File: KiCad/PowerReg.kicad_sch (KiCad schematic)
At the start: 5 parts, among them U2 TPS62162DSG

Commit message: did I really just do the whole thing in one commit
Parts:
- removed R6: 100k, Resistor_SMD:R_0402_1005Metric, symbol Device:R
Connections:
- net PG is gone; now on net GND: U2.8 (PG)
- net +BATT renamed +VDC
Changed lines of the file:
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@@
 	(paper "A4")
+	(junction
+		(at 123.19 77.47)
+		(diameter 0)
+		(color 0 0 0 0)
+	)
+	(junction
+		(at 120.65 77.47)
+		(diameter 0)
+		(color 0 0 0 0)
+	)
+	(junction
+		(at 175.26 63.5)
+		(diameter 0)
+		(color 0 0 0 0)
+	)
+	(junction
+		(at 143.51 57.15)
+		(diameter 0)
+		(color 0 0 0 0)
+	)
+	(junction
+		(at 175.26 55.88)
+		(diameter 0)
+		(color 0 0 0 0)
+	)
 	(junction
 		(at 100.33 57.15)
@@
 		(color 0 0 0 0)
 	)
-	(junction
-		(at 123.19 77.47)
-		(diameter 0)
-		(color 0 0 0 0)
-	)
-	(junction
-		(at 120.65 77.47)
-		(diameter 0)
-		(color 0 0 0 0)
-	)
-	(junction
-		(at 175.26 63.5)
-		(diameter 0)
-		(color 0 0 0 0)
-	)
-	(junction
-		(at 143.51 59.69)
-		(diameter 0)
-		(color 0 0 0 0)
-	)
-	(junction
-		(at 143.51 57.15)
-		(diameter 0)
-		(color 0 0 0 0)
-	)
-	(junction
-		(at 175.26 55.88)
-		(diameter 0)
-		(color 0 0 0 0)
-	)
 	(wire
 		(pts
@@
 	(wire
 		(pts
-			(xy 143.51 71.12) (xy 143.51 67.31)
-		)
-		(stroke
-			(width 0)
-			(type default)
-		)
-	)
-	(wire
-		(pts
 			(xy 123.19 74.93) (xy 123.19 77.47)
 		)
@@
 	(wire
 		(pts
-			(xy 111.76 67.31) (xy 113.03 67.31)
-		)
-		(stroke
-			(width 0)
-			(type default)
-		)
-	)
-	(wire
-		(pts
 			(xy 143.51 57.15) (xy 143.51 59.69)
 		)
@@
 		)
 	)
-	(label "PG"
-		(at 143.51 69.85 0)
-		(effects
-			(font
-				(size 1.27 1.27)
-			)
-			(justify left bottom)
-		)
-	)
-	(label "PG"
-		(at 111.76 67.31 0)
-		(effects
-			(font
-				(size 1.27 1.27)
-			)
-			(justify left bottom)
-		)
-	)
 	(symbol
-		(lib_id "Device:R")
-		(at 143.51 63.5 0)
+		(lib_id "power:GND")
+		(at 113.03 67.31 270)
 		(unit 1)
 		(exclude_from_sim no)
@@
 		(dnp no)
 		(fields_autoplaced yes)
-		(property "Reference" "R6"
-			(at 146.05 62.2299 0)
-			(effects
-				(font
-					(size 1.27 1.27)
-				)
-				(justify left)
-			)
-		)
-		(property "Value" "100k"
-			(at 146.05 64.7699 0)
-			(effects
-				(font
-					(size 1.27 1.27)
-				)
-				(justify left)
-			)
-		)
-		(property "Footprint" "Resistor_SMD:R_0402_1005Metric"
-			(at 141.732 63.5 90)
-			(effects
-				(font
-					(size 1.27 1.27)
-				)
-				(hide yes)
-			)
-		)
-		(property "Datasheet" "~"
-			(at 143.51 63.5 0)
-			(effects
-				(font
-					(size 1.27 1.27)
-				)
-				(hide yes)
-			)
-		)
-		(property "Description" "Resistor"
-			(at 143.51 63.5 0)
+		(property "Reference" "#PWR040"
+			(at 106.68 67.31 0)
+			(effects
+				(font
+					(size 1.27 1.27)
+				)
+				(hide yes)
+			)
+		)
+		(property "Value" "GND"
+			(at 109.22 67.3099 90)
+			(effects
+				(font
+					(size 1.27 1.27)
+				)
+				(justify right)
+			)
+		)
+		(property "Footprint" ""
+			(at 113.03 67.31 0)
+			(effects
+				(font
+					(size 1.27 1.27)
+				)
+				(hide yes)
+			)
+		)
+		(property "Datasheet" ""
+			(at 113.03 67.31 0)
+			(effects
+				(font
+					(size 1.27 1.27)
+				)
+				(hide yes)
+			)
+		)
+		(property "Description" "Power symbol creates a global label with name \"GND\" , ground"
+			(at 113.03 67.31 0)
 			(effects
 				(font
@@
 		(pin "1"
 		)
-		(pin "2"
-		)
 		(instances
-			(project "PowerReg"
+			(project ""
 				(path "/16f8cce7-467e-4342-b55a-00af81cd6f69/bf62daab-1cf5-4742-a85c-ffd3166ecdf9"
-					(reference "R6")
-					(unit 1)
-				)
-			)
-			(project "PowerReg"
-				(path "/69b89bc5-ef32-4b14-b574-fcede0ff2705"
-					(reference "R2")
+					(reference "#PWR040")
 					(unit 1)
 				)
@@
 	)
 	(symbol
-		(lib_id "power:+BATT")
+		(lib_id "power:+VDC")
 		(at 96.52 57.15 0)
 		(unit 1)
@@
 		(on_board yes)
 		(dnp no)
+		(fields_autoplaced yes)
 		(property "Reference" "#PWR033"
-			(at 96.52 60.96 0)
-			(effects
-				(font
-					(size 1.27 1.27)
-				)
-				(hide yes)
-			)
-		)
-		(property "Value" "+BATT"
-			(at 93.98 52.324 0)
+			(at 96.52 59.69 0)
+			(effects
+				(font
+					(size 1.27 1.27)
+				)
+				(hide yes)
+			)
+		)
+		(property "Value" "+VDC"
+			(at 96.52 49.53 0)
 			(effects
 				(font
@@
 			)
 		)
-		(property "Description" "Power symbol creates a global label with name \"+BATT\""
+		(property "Description" "Power symbol creates a global label with name \"+VDC\""
 			(at 96.52 57.15 0)
 			(effects
@@
 				(path "/16f8cce7-467e-4342-b55a-00af81cd6f69/bf62daab-1cf5-4742-a85c-ffd3166ecdf9"
 					(reference "#PWR033")
-					(unit 1)
-				)
-			)
-			(project ""
-				(path "/69b89bc5-ef32-4b14-b574-fcede0ff2705"
-					(reference "#PWR02")
 					(unit 1)
 				)
@@
 	)
 	(symbol
-		(lib_id "power:+BATT")
-		(at 100.33 57.15 0)
-		(unit 1)
-		(exclude_from_sim no)
-		(in_bom yes)
-		(on_board yes)
-		(dnp no)
-		(fields_autoplaced yes)
-		(property "Reference" "#PWR034"
-			(at 100.33 60.96 0)
-			(effects
-				(font
-					(size 1.27 1.27)
-				)
-				(hide yes)
-			)
-		)
-		(property "Value" "+BATT"
-			(at 100.33 52.07 0)
-			(effects
-				(font
-					(size 1.27 1.27)
-				)
-			)
-		)
-		(property "Footprint" ""
-			(at 100.33 57.15 0)
-			(effects
-				(font
-					(size 1.27 1.27)
-				)
-				(hide yes)
-			)
-		)
-		(property "Datasheet" ""
-			(at 100.33 57.15 0)
-			(effects
-				(font
-					(size 1.27 1.27)
-				)
-				(hide yes)
-			)
-		)
-		(property "Description" "Power symbol creates a global label with name \"+BATT\""
-			(at 100.33 57.15 0)
-			(effects
-				(font
-					(size 1.27 1.27)
-				)
-				(hide yes)
-			)
-		)
-		(pin "1"
-		)
-		(instances
-			(project ""
-				(path "/16f8cce7-467e-4342-b55a-00af81cd6f69/bf62daab-1cf5-4742-a85c-ffd3166ecdf9"
-					(reference "#PWR034")
-					(unit 1)
-				)
-			)
-			(project ""
-				(path "/69b89bc5-ef32-4b14-b574-fcede0ff2705"
-					(reference "#PWR04")
-					(unit 1)
-				)
-			)
-		)
-	)
-	(symbol
 		(lib_id "Device:C")
 		(at 175.26 59.69 0)
@@
 					(unit 1)
 				)
+			)
+		)
+	)
+	(symbol
+		(lib_id "power:+VDC")
+		(at 100.33 57.15 0)
+		(unit 1)
+		(exclude_from_sim no)
+		(in_bom yes)
+		(on_board yes)
+		(dnp no)
+		(fields_autoplaced yes)
+		(property "Reference" "#PWR034"
+			(at 100.33 59.69 0)
+			(effects
+				(font
+					(size 1.27 1.27)
+				)
+				(hide yes)
+			)
+		)
+		(property "Value" "+VDC"
+			(at 100.33 49.53 0)
+			(effects
+				(font
+					(size 1.27 1.27)
+				)
+			)
+		)
+		(property "Footprint" ""
+			(at 100.33 57.15 0)
+			(effects
+				(font
+					(size 1.27 1.27)
+				)
+				(hide yes)
+			)
+		)
+		(property "Datasheet" ""
+			(at 100.33 57.15 0)
+			(effects
+				(font
+					(size 1.27 1.27)
+				)
+				(hide yes)
+			)
+		)
+		(property "Description" "Power symbol creates a global label with name \"+VDC\""
+			(at 100.33 57.15 0)
+			(effects
+				(font
+					(size 1.27 1.27)
+				)
+				(hide yes)
+			)
+		)
+		(pin "1"
+		)
+		(instances
+			(project ""
+				(path "/16f8cce7-467e-4342-b55a-00af81cd6f69/bf62daab-1cf5-4742-a85c-ffd3166ecdf9"
+					(reference "#PWR034")
+					(unit 1)
+				)

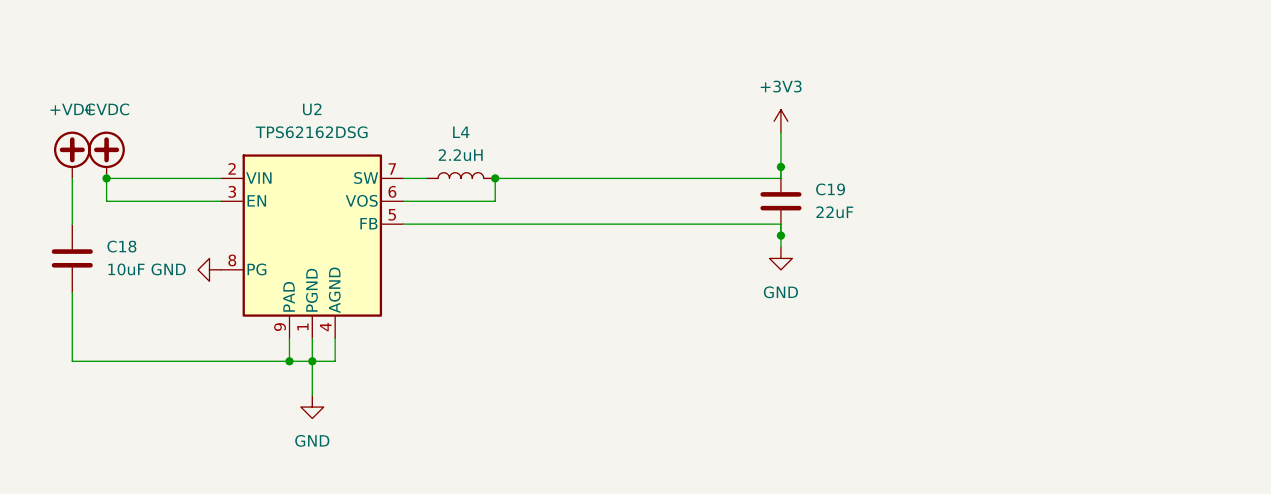
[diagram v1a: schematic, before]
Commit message: tighten up layout, swap out USB connector
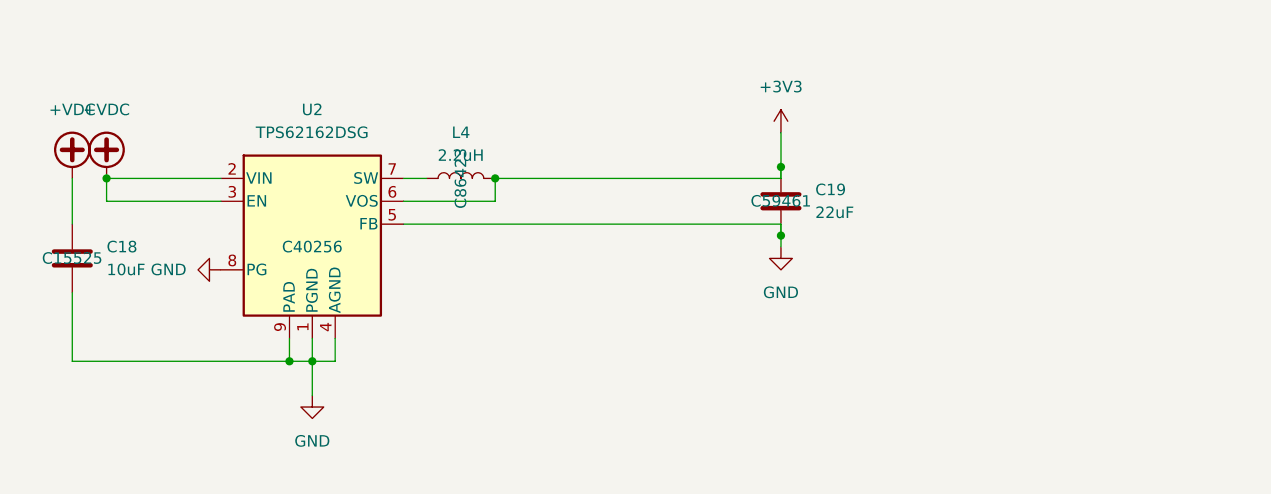
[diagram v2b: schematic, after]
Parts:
- C18: footprint Capacitor_SMD:C_0603_1608Metric -> Capacitor_SMD:C_0402_1005Metric; LCSC (none) -> C15525
- C19: LCSC (none) -> C59461
- L4: LCSC (none) -> C86423
- U2: LCSC (none) -> C40256
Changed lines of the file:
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@@
+	)
+	(junction
+		(at 143.51 57.15)
+		(diameter 0)
+		(color 0 0 0 0)
 	)
 	(junction
@@
 	)
 	(junction
-		(at 143.51 57.15)
-		(diameter 0)
-		(color 0 0 0 0)
-	)
-	(junction
 		(at 175.26 55.88)
 		(diameter 0)
@@
 	(wire
 		(pts
+			(xy 100.33 59.69) (xy 113.03 59.69)
+		)
+		(stroke
+			(width 0)
+			(type default)
+		)
+	)
+	(wire
+		(pts
+			(xy 123.19 74.93) (xy 123.19 77.47)
+		)
+		(stroke
+			(width 0)
+			(type default)
+		)
+	)
+	(wire
+		(pts
+			(xy 133.35 59.69) (xy 143.51 59.69)
+		)
+		(stroke
+			(width 0)
+			(type default)
+		)
+	)
+	(wire
+		(pts
+			(xy 133.35 57.15) (xy 135.89 57.15)
+		)
+		(stroke
+			(width 0)
+			(type default)
+		)
+	)
+	(wire
+		(pts
+			(xy 96.52 57.15) (xy 96.52 62.23)
+		)
+		(stroke
+			(width 0)
+			(type default)
+		)
+	)
+	(wire
+		(pts
+			(xy 125.73 77.47) (xy 125.73 74.93)
+		)
+		(stroke
+			(width 0)
+			(type default)
+		)
+	)
+	(wire
+		(pts
+			(xy 120.65 77.47) (xy 123.19 77.47)
+		)
+		(stroke
+			(width 0)
+			(type default)
+		)
+	)
+	(wire
+		(pts
+			(xy 120.65 74.93) (xy 120.65 77.47)
+		)
+		(stroke
+			(width 0)
+			(type default)
+		)
+	)
+	(wire
+		(pts
 			(xy 175.26 62.23) (xy 175.26 63.5)
 		)
@@
 	(wire
 		(pts
-			(xy 100.33 59.69) (xy 113.03 59.69)
-		)
-		(stroke
-			(width 0)
-			(type default)
-		)
-	)
-	(wire
-		(pts
-			(xy 123.19 74.93) (xy 123.19 77.47)
-		)
-		(stroke
-			(width 0)
-			(type default)
-		)
-	)
-	(wire
-		(pts
-			(xy 133.35 59.69) (xy 143.51 59.69)
-		)
-		(stroke
-			(width 0)
-			(type default)
-		)
-	)
-	(wire
-		(pts
-			(xy 133.35 57.15) (xy 135.89 57.15)
-		)
-		(stroke
-			(width 0)
-			(type default)
-		)
-	)
-	(wire
-		(pts
-			(xy 96.52 57.15) (xy 96.52 62.23)
-		)
-		(stroke
-			(width 0)
-			(type default)
-		)
-	)
-	(wire
-		(pts
-			(xy 125.73 77.47) (xy 125.73 74.93)
-		)
-		(stroke
-			(width 0)
-			(type default)
-		)
-	)
-	(wire
-		(pts
-			(xy 120.65 77.47) (xy 123.19 77.47)
-		)
-		(stroke
-			(width 0)
-			(type default)
-		)
-	)
-	(wire
-		(pts
-			(xy 120.65 74.93) (xy 120.65 77.47)
+			(xy 96.52 77.47) (xy 120.65 77.47)
+		)
+		(stroke
+			(width 0)
+			(type default)
+		)
+	)
+	(wire
+		(pts
+			(xy 123.19 77.47) (xy 125.73 77.47)
+		)
+		(stroke
+			(width 0)
+			(type default)
+		)
+	)
+	(wire
+		(pts
+			(xy 175.26 52.07) (xy 175.26 55.88)
+		)
+		(stroke
+			(width 0)
+			(type default)
+		)
+	)
+	(wire
+		(pts
+			(xy 100.33 57.15) (xy 100.33 59.69)
+		)
+		(stroke
+			(width 0)
+			(type default)
+		)
+	)
+	(wire
+		(pts
+			(xy 143.51 57.15) (xy 175.26 57.15)
+		)
+		(stroke
+			(width 0)
+			(type default)
+		)
+	)
+	(wire
+		(pts
+			(xy 143.51 57.15) (xy 143.51 59.69)
 		)
 		(stroke
@@
 		(pts
 			(xy 175.26 63.5) (xy 175.26 64.77)
-		)
-		(stroke
-			(width 0)
-			(type default)
-		)
-	)
-	(wire
-		(pts
-			(xy 96.52 77.47) (xy 120.65 77.47)
-		)
-		(stroke
-			(width 0)
-			(type default)
-		)
-	)
-	(wire
-		(pts
-			(xy 123.19 77.47) (xy 125.73 77.47)
-		)
-		(stroke
-			(width 0)
-			(type default)
-		)
-	)
-	(wire
-		(pts
-			(xy 175.26 52.07) (xy 175.26 55.88)
-		)
-		(stroke
-			(width 0)
-			(type default)
-		)
-	)
-	(wire
-		(pts
-			(xy 100.33 57.15) (xy 100.33 59.69)
-		)
-		(stroke
-			(width 0)
-			(type default)
-		)
-	)
-	(wire
-		(pts
-			(xy 143.51 57.15) (xy 175.26 57.15)
-		)
-		(stroke
-			(width 0)
-			(type default)
-		)
-	)
-	(wire
-		(pts
-			(xy 143.51 57.15) (xy 143.51 59.69)
 		)
 		(stroke
@@
 			)
 		)
+		(property "LCSC" "C40256"
+			(at 123.19 64.77 0)
+			(effects
+				(font
+					(size 1.27 1.27)
+				)
+			)
+		)
 		(pin "6"
 		)
@@
 			)
 		)
+		(property "LCSC" "C86423"
+			(at 139.7 57.15 0)
+			(effects
+				(font
+					(size 1.27 1.27)
+				)
+			)
+		)
 		(pin "2"
 		)
@@
 			)
 		)
-		(property "Footprint" "Capacitor_SMD:C_0603_1608Metric"
+		(property "Footprint" "Capacitor_SMD:C_0402_1005Metric"
 			(at 97.4852 69.85 0)
 			(effects
@@
 				)
 				(hide yes)
+			)
+		)
+		(property "LCSC" "C15525"
+			(at 96.52 66.04 0)
+			(effects
+				(font
+					(size 1.27 1.27)
+				)
 			)
 		)
@@
 			)
 		)
+		(property "LCSC" "C59461"
+			(at 175.26 59.69 0)
+			(effects
+				(font
+					(size 1.27 1.27)
+				)
+			)
+		)

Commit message: fixed a couple issues
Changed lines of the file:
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@@
 	(paper "A4")
+	(junction
+		(at 110.49 57.15)
+		(diameter 0)
+		(color 0 0 0 0)
+	)
 	(junction
 		(at 123.19 77.47)
@@
 	)
 	(junction
+		(at 96.52 57.15)
+		(diameter 0)
+		(color 0 0 0 0)
+	)
+	(junction
 		(at 175.26 55.88)
 		(diameter 0)
 		(color 0 0 0 0)
 	)
-	(junction
-		(at 100.33 57.15)
-		(diameter 0)
-		(color 0 0 0 0)
-	)
 	(wire
 		(pts
@@
 	(wire
 		(pts
-			(xy 100.33 59.69) (xy 113.03 59.69)
-		)
-		(stroke
-			(width 0)
-			(type default)
-		)
-	)
-	(wire
-		(pts
 			(xy 123.19 74.93) (xy 123.19 77.47)
 		)
@@
 	(wire
 		(pts
+			(xy 110.49 67.31) (xy 110.49 68.58)
+		)
+		(stroke
+			(width 0)
+			(type default)
+		)
+	)
+	(wire
+		(pts
 			(xy 175.26 62.23) (xy 175.26 63.5)
 		)
@@
 	(wire
 		(pts
-			(xy 100.33 57.15) (xy 100.33 59.69)
+			(xy 113.03 59.69) (xy 110.49 59.69)
 		)
 		(stroke
@@
 	(wire
 		(pts
+			(xy 110.49 57.15) (xy 113.03 57.15)
+		)
+		(stroke
+			(width 0)
+			(type default)
+		)
+	)
+	(wire
+		(pts
 			(xy 143.51 57.15) (xy 143.51 59.69)
 		)
@@
 	(wire
 		(pts
-			(xy 100.33 57.15) (xy 113.03 57.15)
+			(xy 110.49 67.31) (xy 113.03 67.31)
+		)
+		(stroke
+			(width 0)
+			(type default)
+		)
+	)
+	(wire
+		(pts
+			(xy 96.52 57.15) (xy 110.49 57.15)
+		)
+		(stroke
+			(width 0)
+			(type default)
+		)
+	)
+	(wire
+		(pts
+			(xy 110.49 59.69) (xy 110.49 57.15)
 		)
 		(stroke
@@
 	(symbol
 		(lib_id "power:GND")
-		(at 113.03 67.31 270)
+		(at 110.49 68.58 0)
 		(unit 1)
 		(exclude_from_sim no)
@@
 		(on_board yes)
 		(dnp no)
-		(fields_autoplaced yes)
 		(property "Reference" "#PWR040"
-			(at 106.68 67.31 0)
+			(at 110.49 74.93 0)
 			(effects
 				(font
@@
 		)
 		(property "Value" "GND"
-			(at 109.22 67.3099 90)
-			(effects
-				(font
-					(size 1.27 1.27)
-				)
-				(justify right)
+			(at 108.712 72.644 0)
+			(effects
+				(font
+					(size 1.27 1.27)
+				)
+				(justify left)
 			)
 		)
 		(property "Footprint" ""
-			(at 113.03 67.31 0)
+			(at 110.49 68.58 0)
 			(effects
 				(font
@@
 		)
 		(property "Datasheet" ""
-			(at 113.03 67.31 0)
+			(at 110.49 68.58 0)
 			(effects
 				(font
@@
 		)
 		(property "Description" "Power symbol creates a global label with name \"GND\" , ground"
-			(at 113.03 67.31 0)
+			(at 110.49 68.58 0)
 			(effects
 				(font
@@
 		(on_board yes)
 		(dnp no)
-		(fields_autoplaced yes)
 		(property "Reference" "L4"
 			(at 139.7 52.07 90)
@@
 		)
 		(property "LCSC" "C86423"
-			(at 139.7 57.15 0)
+			(at 139.7 57.15 90)
 			(effects
 				(font
@@
 					(unit 1)
 				)
-			)
-		)
-	)
-	(symbol
-		(lib_id "power:+VDC")
-		(at 100.33 57.15 0)
-		(unit 1)
-		(exclude_from_sim no)
-		(in_bom yes)
-		(on_board yes)
-		(dnp no)
-		(fields_autoplaced yes)
-		(property "Reference" "#PWR034"
-			(at 100.33 59.69 0)
-			(effects
-				(font
-					(size 1.27 1.27)
-				)
-				(hide yes)
-			)
-		)
-		(property "Value" "+VDC"
-			(at 100.33 49.53 0)
-			(effects
-				(font
-					(size 1.27 1.27)
-				)
-			)
-		)
-		(property "Footprint" ""
-			(at 100.33 57.15 0)
-			(effects
-				(font
-					(size 1.27 1.27)
-				)
-				(hide yes)
-			)
-		)
-		(property "Datasheet" ""
-			(at 100.33 57.15 0)
-			(effects
-				(font
-					(size 1.27 1.27)
-				)
-				(hide yes)
-			)
-		)
-		(property "Description" "Power symbol creates a global label with name \"+VDC\""
-			(at 100.33 57.15 0)
-			(effects
-				(font
-					(size 1.27 1.27)
-				)
-				(hide yes)
-			)
-		)
-		(pin "1"
-		)
-		(instances
-			(project ""
-				(path "/16f8cce7-467e-4342-b55a-00af81cd6f69/bf62daab-1cf5-4742-a85c-ffd3166ecdf9"
-					(reference "#PWR034")
-					(unit 1)
-				)

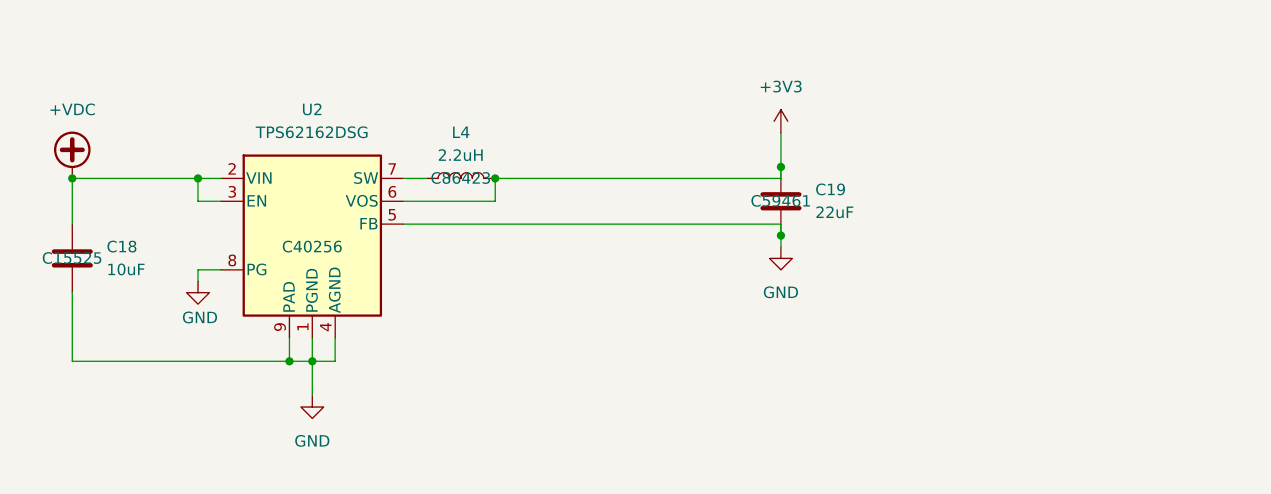
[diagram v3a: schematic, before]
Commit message: switch to double diode and add beeper
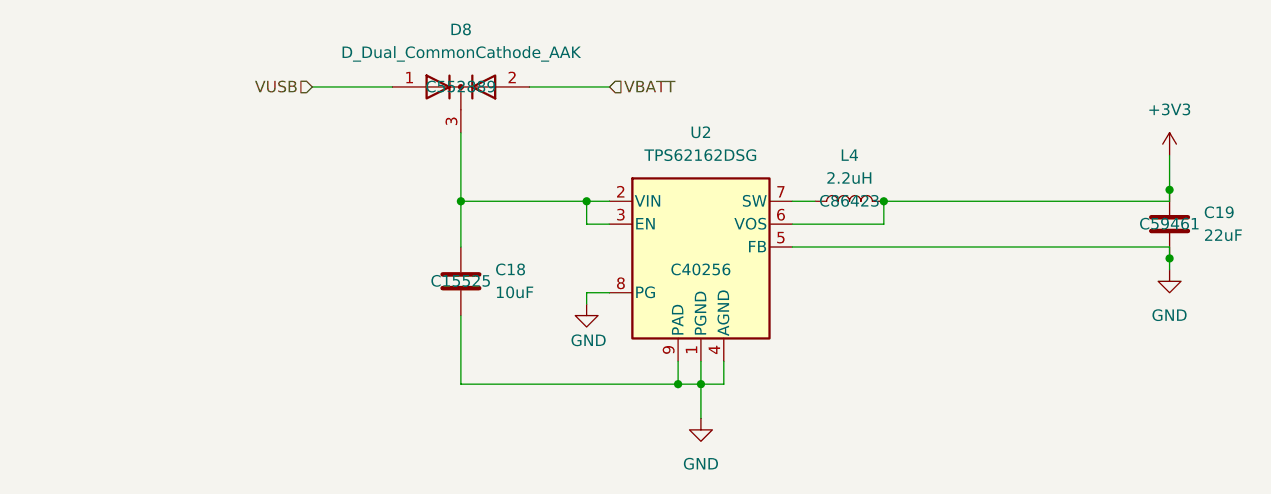
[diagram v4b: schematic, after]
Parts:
- added D8: D_Dual_CommonCathode_AAK, Package_TO_SOT_SMD:TSOT-23, symbol Device:D_Dual_CommonCathode_AAK
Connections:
- net +VDC: no longer names the net of C18.1, U2.2 (VIN), U2.3 (EN)
- net +VDC: now also D8.3 (K)
- new net VBATT: D8.2 (A)
- new net VUSB: D8.1 (A)
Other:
- moved on the sheet: C18, C19, L4, U2
